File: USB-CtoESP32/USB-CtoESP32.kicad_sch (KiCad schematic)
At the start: 24 parts, among them J1 USB_C_Receptacle_USB2.0_14P, J2 Conn_01x04_Pin, U1 LM1117MP-3.3, U2 CH340G, Y1 12MHz

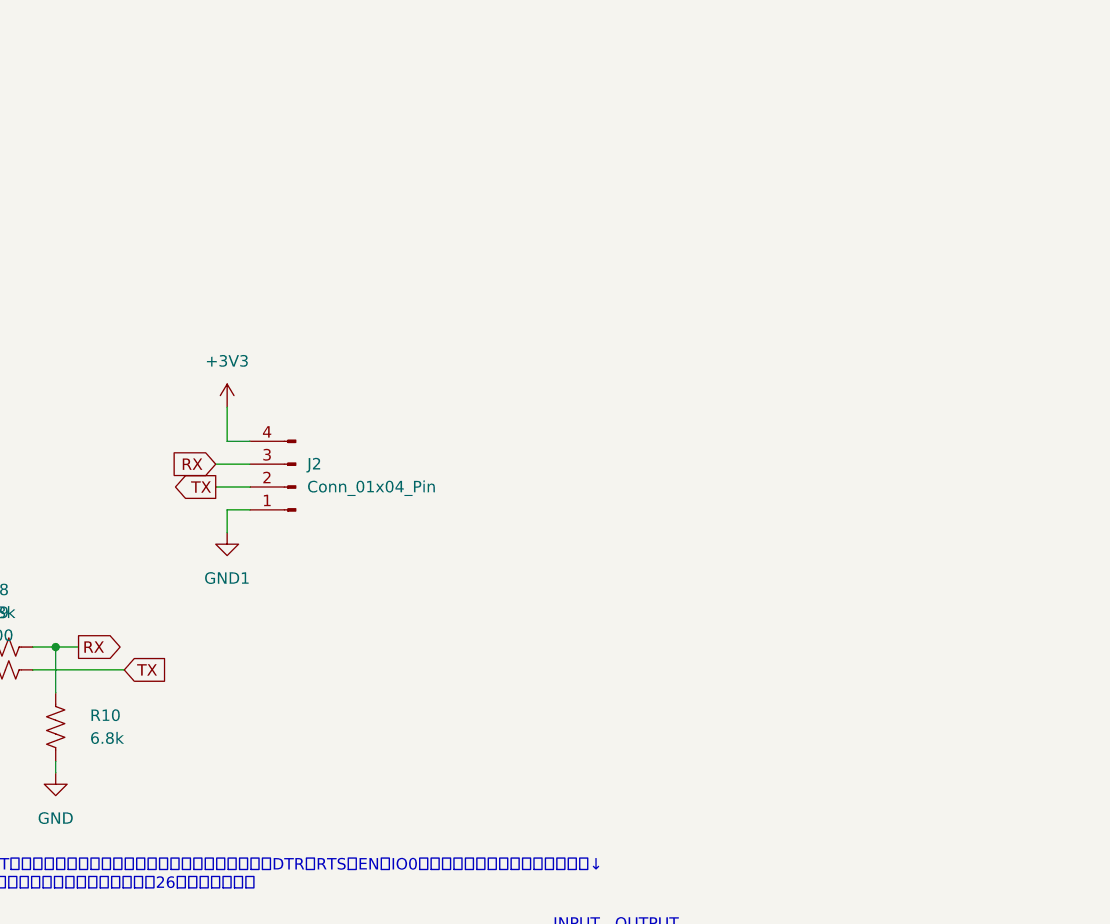
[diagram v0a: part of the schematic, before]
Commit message: Add files via upload
ENとIO0を追加
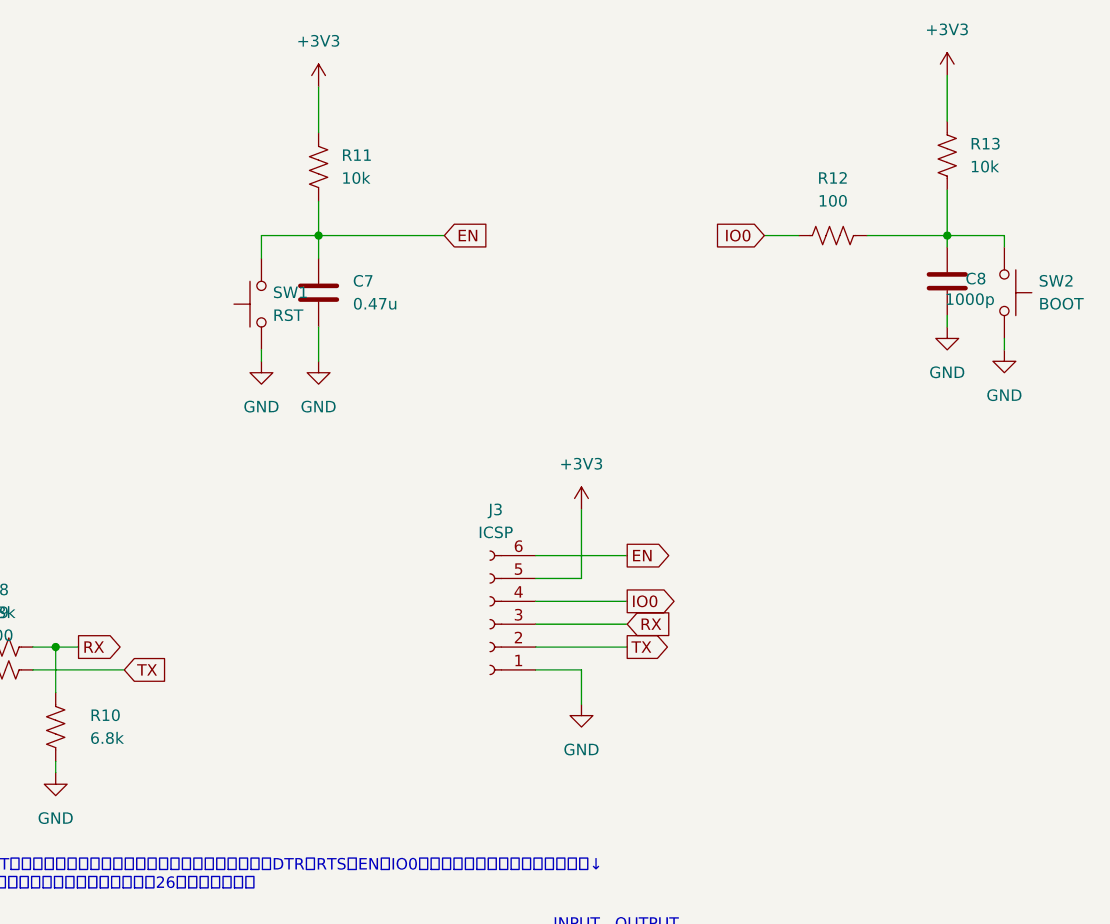
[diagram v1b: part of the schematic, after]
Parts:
- removed J2: Conn_01x04_Pin, Connector_PinHeader_2.54mm:PinHeader_1x04_P2.54mm_Horizontal, symbol Connector:Conn_01x04_Pin
- added C7: 0.47u, Capacitor_SMD:C_0603_1608Metric, symbol Device:C
- added C8: 1000p, Capacitor_SMD:C_0603_1608Metric, symbol Device:C
- added J3: ICSP, Connector_PinHeader_2.54mm:PinHeader_2x03_P2.54mm_Vertical, symbol Connector:Conn_01x06_Socket
- added R11, R13: 10k, Resistor_SMD:R_0603_1608Metric, symbol Device:R_US
- added R12: 100, Resistor_SMD:R_0603_1608Metric, symbol Device:R_US
- added SW1: RST, Button_Switch_SMD:SW_SPST_PTS810, symbol Switch:SW_Push
- added SW2: BOOT, Button_Switch_SMD:SW_SPST_PTS810, symbol Switch:SW_Push
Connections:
- net +3V3: now also J3.5 (Pin_5), R11.1, R13.1
- net GND: now also C7.2, C8.2, J3.1 (Pin_1), SW1.1, SW2.2
- net RX: now also J3.3 (Pin_3)
- net TX: now also J3.2 (Pin_2)
- new net: C8.1, R12.2, R13.2, SW2.1
- new net EN: C7.1, J3.6 (Pin_6), R11.2, SW1.2
- new net IO0: J3.4 (Pin_4), R12.1

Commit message: Add files via upload
配線終了。
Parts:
- C1, C2, C4: footprint Capacitor_SMD:C_1206_3216Metric -> Capacitor_SMD:C_0603_1608Metric
- J3: footprint Connector_PinHeader_2.54mm:PinHeader_2x03_P2.54mm_Vertical -> Connector_PinHeader_2.54mm:PinHeader_2x03_P2.54mm_Horizontal
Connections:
- net GND: now also C3.1
- net at C3.2, U2.16 (VCC): now also C2.1, D1.1 (K), D2.1 (K), U1.3 (VI)
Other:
- moved on the sheet: C3
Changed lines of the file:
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@@
 (kicad_sch
-	(version 20231120)
+	(version 20250114)
 	(generator "eeschema")
-	(generator_version "8.0")
+	(generator_version "9.0")
 	(paper "A4")
+	(text "BOOTボタンを押さずに書き込めるようにしたかったら、DTR・RTSとEN・IO0の間に論路回路を足す必要あり。↓\n25代から上手くいかなかったため、26代ではやめた。"
+		(exclude_from_sim no)
+		(at 158.75 114.3 0)
+		(effects
+			(font
+				(size 1.27 1.27)
+			)
+			(justify left)
+		)
+	)
+	(text " INPUT   OUTPUT\nDTR RTS  EN  IO0\n 1   1    1   1 \n 0   0    1   1\n 1   0    0   1\n 0   1    1   0"
+		(exclude_from_sim no)
+		(at 230.886 124.968 0)
+		(effects
+			(font
+				(size 1.27 1.27)
+			)
+		)
+	)
 	(junction
 		(at 121.92 67.31)
@@
 	)
 	(junction
+		(at 118.11 83.82)
+		(diameter 0)
+		(color 0 0 0 0)
+	)
+	(junction
 		(at 111.76 93.98)
 		(diameter 0)
@@
 	(wire
 		(pts
-			(xy 129.54 83.82) (xy 118.11 83.82)
-		)
-		(stroke
-			(width 0)
-			(type default)
-		)
-	)
-	(wire
-		(pts
 			(xy 156.21 88.9) (xy 158.75 88.9)
 		)
@@
 	(wire
 		(pts
+			(xy 118.11 83.82) (xy 143.51 83.82)
+		)
+		(stroke
+			(width 0)
+			(type default)
+		)
+	)
+	(wire
+		(pts
 			(xy 267.97 38.1) (xy 267.97 43.18)
 		)
@@
 	(wire
 		(pts
-			(xy 143.51 83.82) (xy 137.16 83.82)
-		)
-		(stroke
-			(width 0)
-			(type default)
-		)
-	)
-	(wire
-		(pts
 			(xy 140.97 77.47) (xy 142.24 77.47)
 		)
@@
 		)
 	)
-	(text "BOOTボタンを押さずに書き込めるようにしたかったら、DTR・RTSとEN・IO0の間に論路回路を足す必要あり。↓\n25代から上手くいかなかったため、26代ではやめた。"
-		(exclude_from_sim no)
-		(at 158.75 114.3 0)
-		(effects
-			(font
-				(size 1.27 1.27)
-			)
-			(justify left)
-		)
-	)
-	(text " INPUT   OUTPUT\nDTR RTS  EN  IO0\n 1   1    1   1 \n 0   0    1   1\n 1   0    0   1\n 0   1    1   0"
-		(exclude_from_sim no)
-		(at 230.886 124.968 0)
-		(effects
-			(font
-				(size 1.27 1.27)
-			)
-		)
-	)
 	(global_label "TX"
 		(shape output)
@@
 			)
 		)
-		(property "Footprint" "Capacitor_SMD:C_1206_3216Metric"
+		(property "Footprint" "Capacitor_SMD:C_0603_1608Metric"
 			(at 122.8852 77.47 0)
 			(effects
@@
 	)
 	(symbol
+		(lib_id "power:GND")
+		(at 118.11 91.44 0)
+		(unit 1)
+		(exclude_from_sim no)
+		(in_bom yes)
+		(on_board yes)
+		(dnp no)
+		(property "Reference" "#PWR020"
+			(at 118.11 97.79 0)
+			(effects
+				(font
+					(size 1.27 1.27)
+				)
+				(hide yes)
+			)
+		)
+		(property "Value" "GND"
+			(at 118.11 94.742 0)
+			(effects
+				(font
+					(size 1.27 1.27)
+				)
+			)
+		)
+		(property "Footprint" ""
+			(at 118.11 91.44 0)
+			(effects
+				(font
+					(size 1.27 1.27)
+				)
+				(hide yes)
+			)
+		)
+		(property "Datasheet" ""
+			(at 118.11 91.44 0)
+			(effects
+				(font
+					(size 1.27 1.27)
+				)
+				(hide yes)
+			)
+		)
+		(property "Description" "Power symbol creates a global label with name \"GND\" , ground"
+			(at 118.11 91.44 0)
+			(effects
+				(font
+					(size 1.27 1.27)
+				)
+				(hide yes)
+			)
+		)
+		(pin "1"
+		)
+		(instances
+			(project "USB-CtoESP32"
+				(path "/36f97cbd-7aa7-4209-89e1-16f43bdb7e21"
+					(reference "#PWR020")
+					(unit 1)
+				)
+			)
+		)
+	)
+	(symbol
 		(lib_id "Device:R_US")
 		(at 127 77.47 90)
@@
 			)
 		)
-		(property "Footprint" "Connector_PinHeader_2.54mm:PinHeader_2x03_P2.54mm_Vertical"
+		(property "Footprint" "Connector_PinHeader_2.54mm:PinHeader_2x03_P2.54mm_Horizontal"
 			(at 217.17 86.36 0)
 			(effects
@@
 	(symbol
 		(lib_id "Device:C")
-		(at 133.35 83.82 90)
+		(at 118.11 87.63 180)
 		(unit 1)
 		(exclude_from_sim no)
@@
 		(fields_autoplaced yes)
 		(property "Reference" "C3"
-			(at 133.35 76.2 90)
+			(at 121.92 86.3599 0)
 			(effects
 				(font
 					(size 1.27 1.27)
 				)
+				(justify right)
 			)
 		)
 		(property "Value" "0.1u"
-			(at 133.35 78.74 90)
+			(at 121.92 88.8999 0)
 			(effects
 				(font
 					(size 1.27 1.27)
 				)
+				(justify right)
 			)
 		)
 		(property "Footprint" "Capacitor_SMD:C_0603_1608Metric"
-			(at 137.16 82.8548 0)
+			(at 117.1448 83.82 0)
 			(effects
 				(font
@@
 		)
 		(property "Datasheet" "~"
-			(at 133.35 83.82 0)
+			(at 118.11 87.63 0)
 			(effects
 				(font
@@
 		)
 		(property "Description" "Unpolarized capacitor"
-			(at 133.35 83.82 0)
+			(at 118.11 87.63 0)
 			(effects
 				(font
@@
 			)
 		)
-		(property "Footprint" "Capacitor_SMD:C_1206_3216Metric"
+		(property "Footprint" "Capacitor_SMD:C_0603_1608Metric"
 			(at 143.2052 77.47 0)
 			(effects
@@
 			)
 		)
-		(property "Footprint" "Capacitor_SMD:C_1206_3216Metric"
+		(property "Footprint" "Capacitor_SMD:C_0603_1608Metric"
 			(at 68.2752 128.27 0)
 			(effects
@@
 		)
 	)
+	(embedded_fonts no)
 )

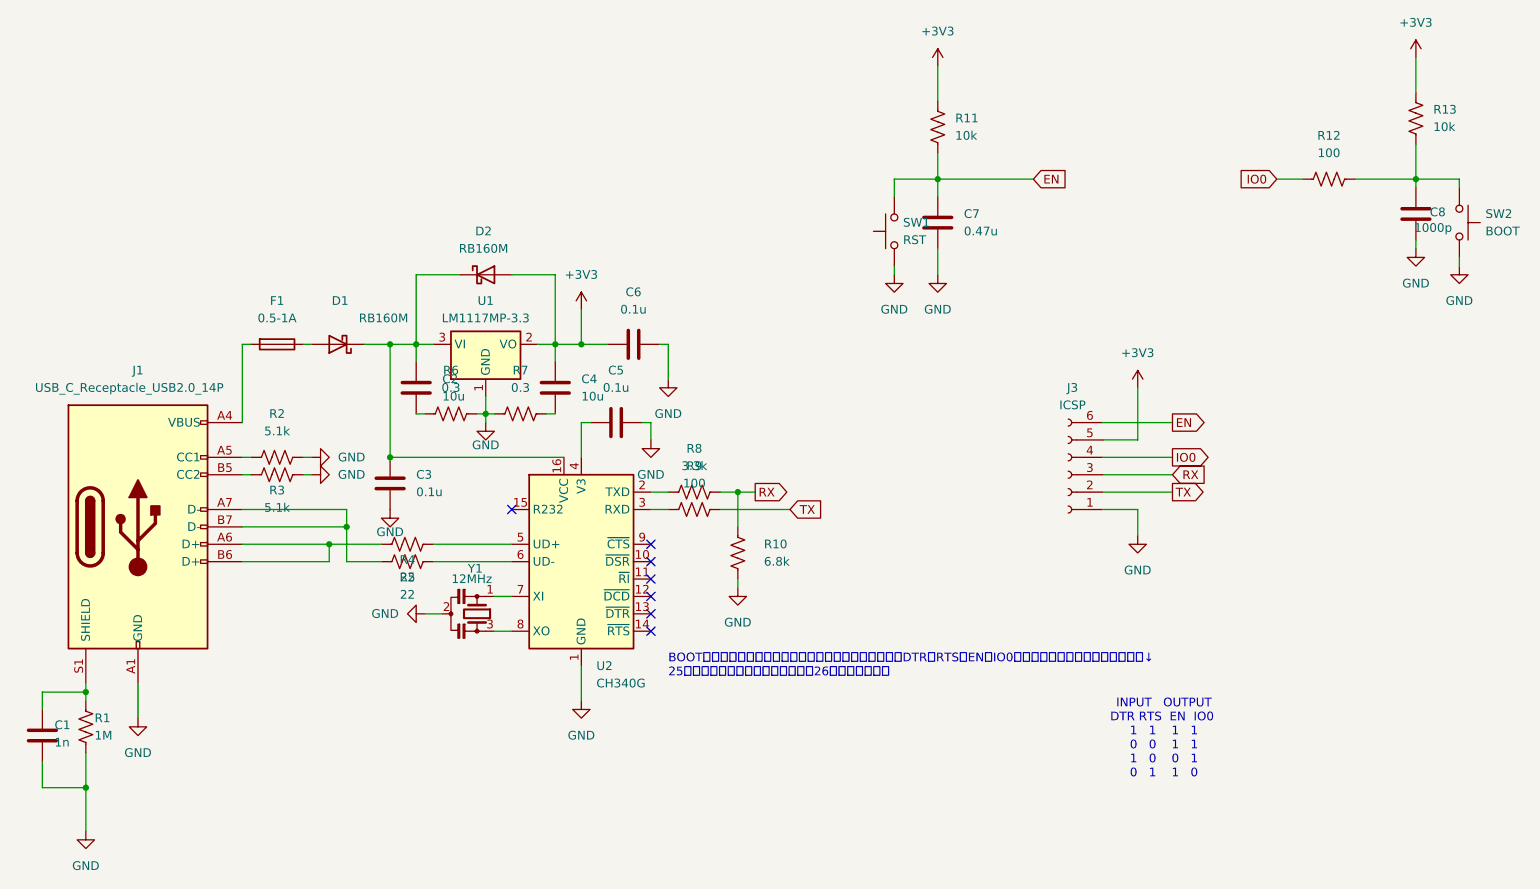
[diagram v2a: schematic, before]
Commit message: Add files via upload
入江さんからのフィードバックを回路図に反映
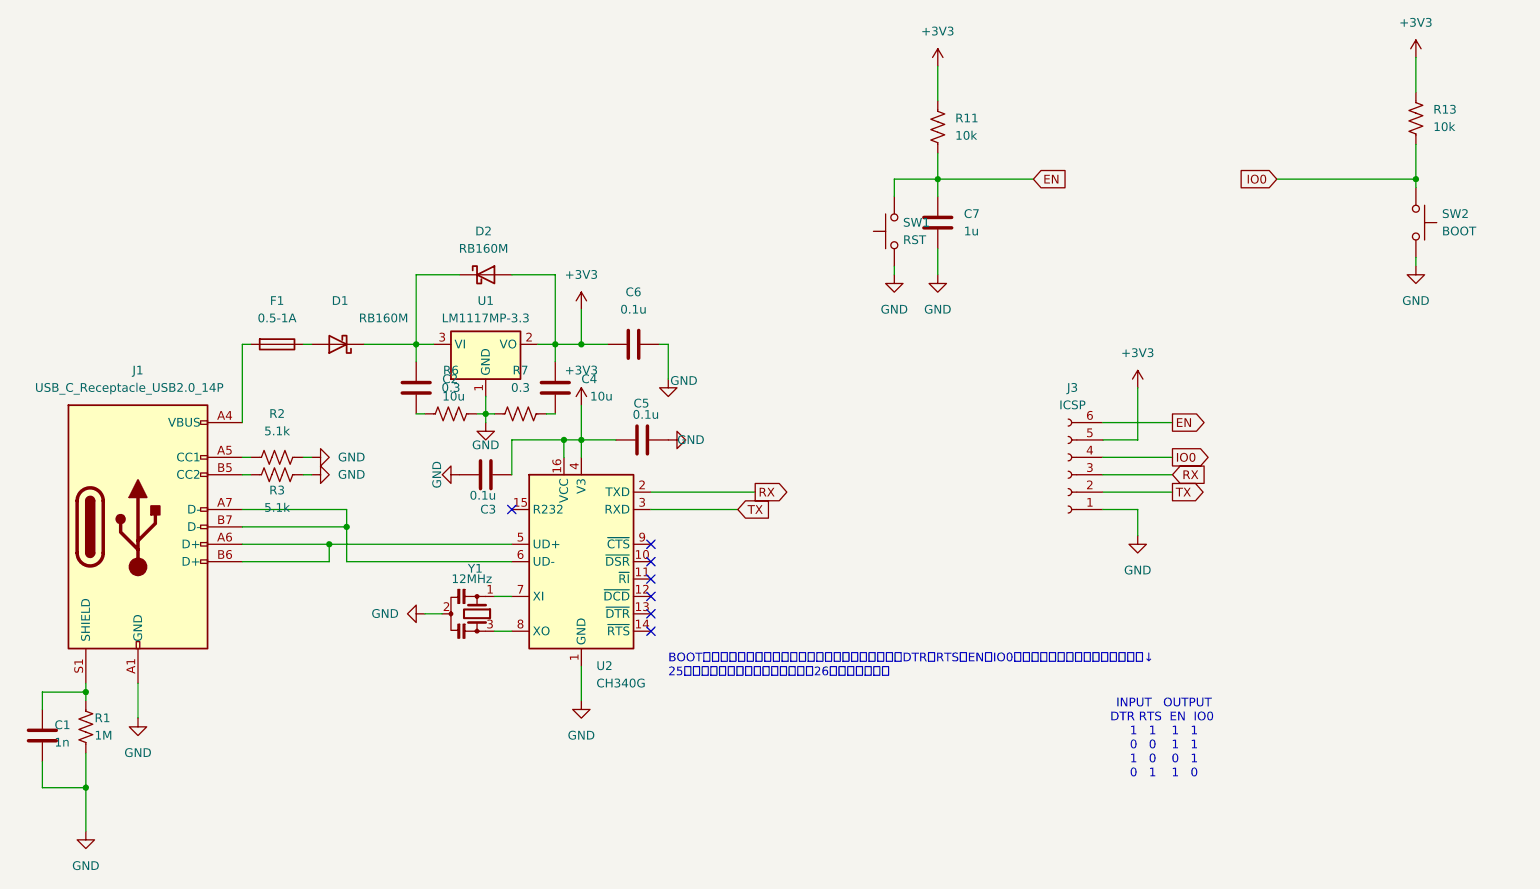
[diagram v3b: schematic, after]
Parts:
- removed C8: 1000p, Capacitor_SMD:C_0603_1608Metric, symbol Device:C
- removed R10: 6.8k, Resistor_SMD:R_0603_1608Metric, symbol Device:R_US
- removed R12, R9: 100, Resistor_SMD:R_0603_1608Metric, symbol Device:R_US
- removed R4, R5: 22, Resistor_SMD:R_0603_1608Metric, symbol Device:R_US
- removed R8: 3.3k, Resistor_SMD:R_0603_1608Metric, symbol Device:R_US
- C7: value 0.47u -> 1u
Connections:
- net +3V3: now also C3.2, C5.2, U2.16 (VCC), U2.4 (V3)
- net GND: now also C5.1; no longer C5.2
- net IO0: now also R13.2, SW2.1
- net RX: now also U2.2 (TXD)
- net TX: now also U2.3 (RXD)
- net at C2.1, D1.1 (K), D2.1 (K)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: no longer C3.2, U2.16 (VCC)
- net at U2.5 (UD+): now also J1.A6 (D+), J1.B6 (D+)
- net at U2.6 (UD-): now also J1.A7 (D-), J1.B7 (D-)
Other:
- moved on the sheet: C3, SW2

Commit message: Add files via upload
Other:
- moved on the sheet: J3
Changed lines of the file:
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@@
 	(wire
 		(pts
-			(xy 222.25 91.44) (xy 227.33 91.44)
-		)
-		(stroke
-			(width 0)
-			(type default)
-		)
-	)
-	(wire
-		(pts
-			(xy 222.25 83.82) (xy 232.41 83.82)
+			(xy 222.25 92.71) (xy 227.33 92.71)
+		)
+		(stroke
+			(width 0)
+			(type default)
+		)
+	)
+	(wire
+		(pts
+			(xy 222.25 85.09) (xy 232.41 85.09)
 		)
 		(stroke
@@
 	(wire
 		(pts
-			(xy 227.33 91.44) (xy 227.33 95.25)
+			(xy 227.33 92.71) (xy 227.33 96.52)
 		)
 		(stroke
@@
 	(wire
 		(pts
-			(xy 222.25 81.28) (xy 227.33 81.28)
+			(xy 222.25 82.55) (xy 227.33 82.55)
 		)
 		(stroke
@@
 	(wire
 		(pts
-			(xy 222.25 86.36) (xy 232.41 86.36)
+			(xy 222.25 87.63) (xy 232.41 87.63)
 		)
 		(stroke
@@
 	(wire
 		(pts
-			(xy 222.25 78.74) (xy 232.41 78.74)
+			(xy 222.25 80.01) (xy 232.41 80.01)
 		)
 		(stroke
@@
 	(wire
 		(pts
-			(xy 227.33 81.28) (xy 227.33 73.66)
+			(xy 227.33 82.55) (xy 227.33 74.93)
 		)
 		(stroke
@@
 	(wire
 		(pts
-			(xy 222.25 88.9) (xy 232.41 88.9)
+			(xy 222.25 90.17) (xy 232.41 90.17)
 		)
 		(stroke
@@
 	(global_label "TX"
 		(shape output)
-		(at 232.41 88.9 0)
+		(at 232.41 90.17 0)
 		(fields_autoplaced yes)
 		(effects
@@
 		)
 		(property "Intersheetrefs" "${INTERSHEET_REFS}"
-			(at 237.5723 88.9 0)
+			(at 237.5723 90.17 0)
 			(effects
 				(font
@@
 	(global_label "EN"
 		(shape output)
-		(at 232.41 78.74 0)
+		(at 232.41 80.01 0)
 		(fields_autoplaced yes)
 		(effects
@@
 		)
 		(property "Intersheetrefs" "${INTERSHEET_REFS}"
-			(at 237.8747 78.74 0)
+			(at 237.8747 80.01 0)
 			(effects
 				(font
@@
 	(global_label "IO0"
 		(shape output)
-		(at 232.41 83.82 0)
+		(at 232.41 85.09 0)
 		(fields_autoplaced yes)
 		(effects
@@
 		)
 		(property "Intersheetrefs" "${INTERSHEET_REFS}"
-			(at 238.54 83.82 0)
+			(at 238.54 85.09 0)
 			(effects
 				(font
@@
 	(global_label "RX"
 		(shape input)
-		(at 232.41 86.36 0)
+		(at 232.41 87.63 0)
 		(fields_autoplaced yes)
 		(effects
@@
 		)
 		(property "Intersheetrefs" "${INTERSHEET_REFS}"
-			(at 237.8747 86.36 0)
+			(at 237.8747 87.63 0)
 			(effects
 				(font
@@
 	(symbol
 		(lib_id "power:+5V")
-		(at 227.33 73.66 0)
+		(at 227.33 74.93 0)
 		(unit 1)
 		(exclude_from_sim no)
@@
 		(fields_autoplaced yes)
 		(property "Reference" "#PWR014"
-			(at 227.33 77.47 0)
+			(at 227.33 78.74 0)
 			(effects
 				(font
@@
 		)
 		(property "Value" "+3V3"
-			(at 227.33 68.58 0)
+			(at 227.33 69.85 0)
 			(effects
 				(font
@@
 		)
 		(property "Footprint" ""
-			(at 227.33 73.66 0)
+			(at 227.33 74.93 0)
 			(effects
 				(font
@@
 		)
 		(property "Datasheet" ""
-			(at 227.33 73.66 0)
+			(at 227.33 74.93 0)
 			(effects
 				(font
@@
 		)
 		(property "Description" "Power symbol creates a global label with name \"+5V\""
-			(at 227.33 73.66 0)
+			(at 227.33 74.93 0)
 			(effects
 				(font
@@
 	(symbol
 		(lib_id "Connector:Conn_01x06_Socket")
-		(at 217.17 86.36 180)
+		(at 217.17 87.63 180)
 		(unit 1)
 		(exclude_from_sim no)
@@
 		(fields_autoplaced yes)
 		(property "Reference" "J3"
-			(at 217.805 73.66 0)
+			(at 217.805 74.93 0)
 			(effects
 				(font
@@
 		)
 		(property "Value" "ICSP"
-			(at 217.805 76.2 0)
+			(at 217.805 77.47 0)
 			(effects
 				(font
@@
 		)
 		(property "Footprint" "Connector_PinHeader_2.54mm:PinHeader_2x03_P2.54mm_Horizontal"
-			(at 217.17 86.36 0)
+			(at 217.17 87.63 0)
 			(effects
 				(font
@@
 		)
 		(property "Datasheet" "~"
-			(at 217.17 86.36 0)
+			(at 217.17 87.63 0)
 			(effects
 				(font
@@
 		)
 		(property "Description" "Generic connector, single row, 01x06, script generated"
-			(at 217.17 86.36 0)
+			(at 217.17 87.63 0)
 			(effects
 				(font
@@
 	(symbol
 		(lib_id "power:GND")
-		(at 227.33 95.25 0)
+		(at 227.33 96.52 0)
 		(unit 1)
 		(exclude_from_sim no)
@@
 		(fields_autoplaced yes)
 		(property "Reference" "#PWR015"
+			(at 227.33 102.87 0)
+			(effects
+				(font
+					(size 1.27 1.27)
+				)
+				(hide yes)
+			)
+		)
+		(property "Value" "GND"
 			(at 227.33 101.6 0)
 			(effects
@@
 					(size 1.27 1.27)
 				)
-				(hide yes)
-			)
-		)
-		(property "Value" "GND"
-			(at 227.33 100.33 0)
-			(effects
-				(font
-					(size 1.27 1.27)
-				)
 			)
 		)
 		(property "Footprint" ""
-			(at 227.33 95.25 0)
+			(at 227.33 96.52 0)
 			(effects
 				(font
@@
 		)
 		(property "Datasheet" ""
-			(at 227.33 95.25 0)
+			(at 227.33 96.52 0)
 			(effects
 				(font
@@
 		)
 		(property "Description" "Power symbol creates a global label with name \"GND\" , ground"
-			(at 227.33 95.25 0)
-			(effects
-				(font
+			(at 227.33 96.52 0)
+			(effects
+				(font
